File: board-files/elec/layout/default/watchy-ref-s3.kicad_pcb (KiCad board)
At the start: 4 copper layers, 33.8 x 46 mm, 70 parts, among them J1 FPC24(0.5MM), J2 Micro USB, J3 Battery, M1 Vibration_Motor, Q1 AO3400A, Q2 UMH3N, Q4 CJ2301, Q5 S8050, SW1 BTN, SW2 BTN, SW3 BTN, SW4 BTN, U1 ESP32-PICO-D4, U2 ME6211C33M5G-N, U3 CP2102, U4 BMA423, U5 TP4054, U6 PCF8563BS, Y1 32.768KHz

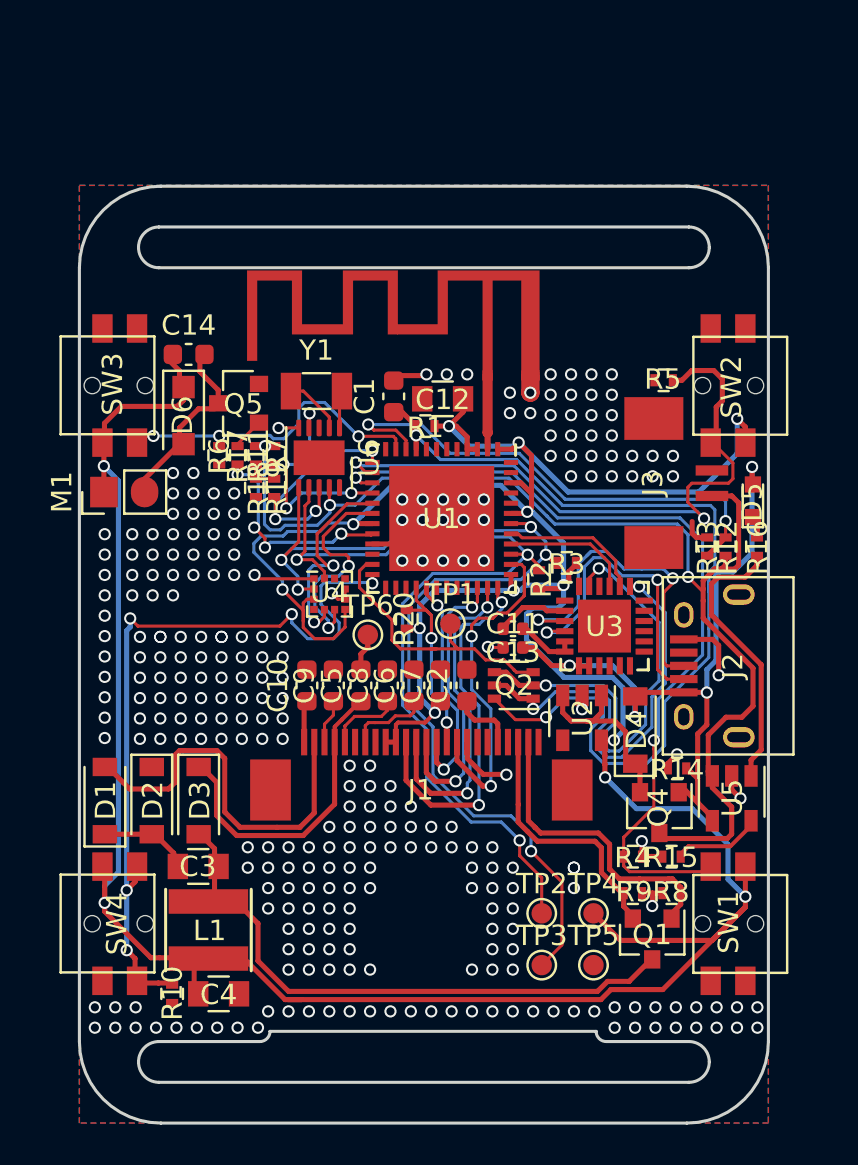
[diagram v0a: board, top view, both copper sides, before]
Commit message: board: apply the netlist to the PCB headlessly, and verify it
KiCad's netlist import is a GUI dialog and kicad-cli has no equivalent, so
scripts/apply_netlist.py does that job with pcbnew. The part that mattered
was preserving placement: V2's footprints carry KiCad 5 library names, so a
naive delete-and-re-add loses V2's coordinates for 39 parts over what is
mostly just a rename. It now records each pose and restores it.

It also adds and places the new parts, assigns all 249 pads across 73 nets,
lays the GND and +3V3 pour outlines, and nudges the small parts it placed
off their neighbours on a spiral search. The module goes 7.7mm below the top
edge so Espressif's antenna keepout -- which forbids pour on every layer --
hangs off the board.

scripts/check_board.py verifies the result independently and is wired into
checks/run.sh. Both it and the netlist assertions are mutation-tested.

Seven courtyard overlaps are left for a human and reported with their depth:
the 15.4x20.5mm module lands on C12, C1, R1, R7 and Q5 where V2 had a 7x7
QFN, and the USB-C lands on D4 and U2. Where those parts move is a design
decision, not arithmetic. Nothing is routed.
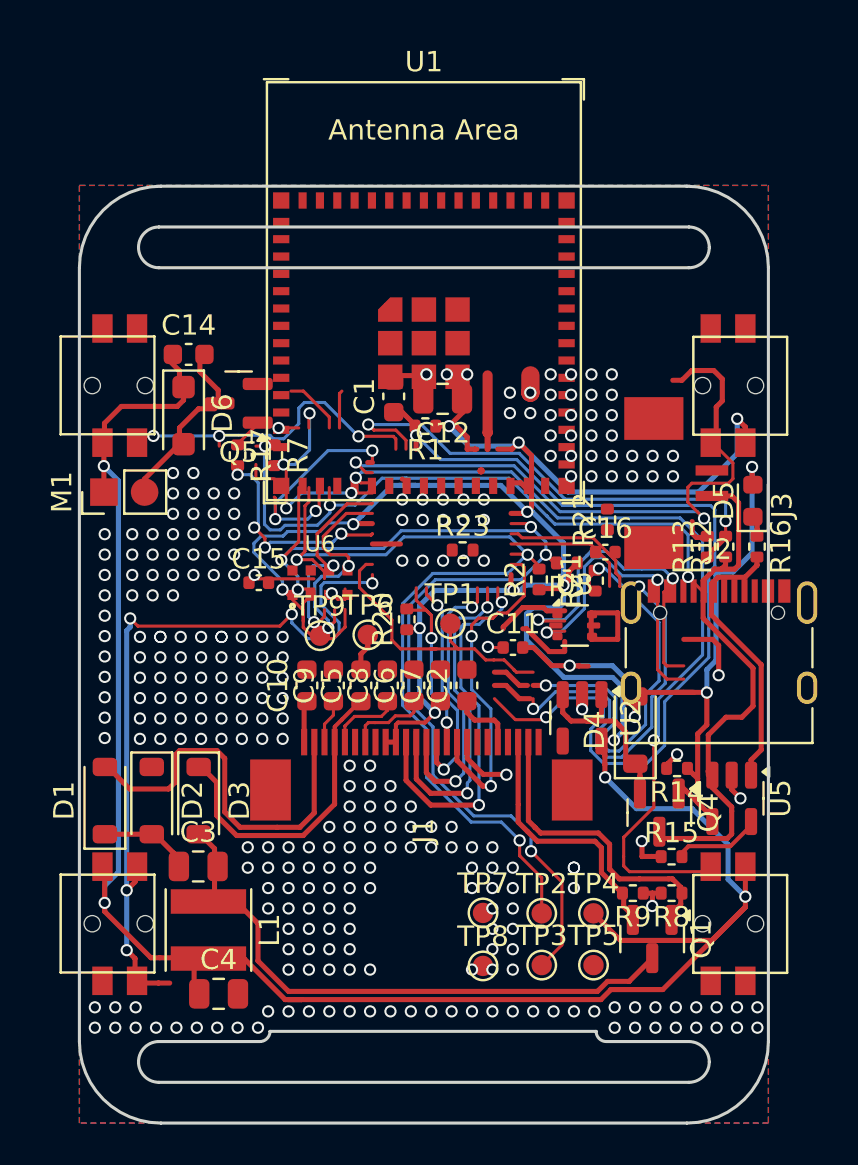
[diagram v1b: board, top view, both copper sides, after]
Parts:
- removed AE1: SWRA117D, Watchy:SWRA117D
- removed C13: 4.7uF, Capacitor_SMD:C_0402_1005Metric
- removed Q2: UMH3N, TO_SOT_Packages_SMD:SOT-363_SC-70-6
- removed R10, R4, R5, R6: 10K, Resistors_SMD:R_0402
- removed R11: 680K, Watchy:R_0402
- removed R18: 220K, Watchy:R_0402
- removed R19: 100K, Watchy:R_0402
- removed U4: BMA423, Housings_LGA:LGA-12_2x2mm_Pitch0.5mm
- removed Y1: 32.768KHz, Crystal:Crystal_SMD_3215-2Pin_3.2x1.5mm
- added C15: 100nF, C_0402_1005Metric, F.Cu at (77.5, 89.6)
- added C16: 100nF, C_0402_1005Metric, F.Cu at (94.5, 88.1)
- added R21: 5.1k, R_0402_1005Metric, F.Cu at (94.0, 89.5)
- added R22: 5.1k, R_0402_1005Metric, F.Cu at (94.6, 86.5)
- added R23: 10k, R_0402_1005Metric, F.Cu at (87.5, 88.0)
- added TP7: 1.0mm test pad, TestPoint_Pad_D1.0mm, F.Cu at (88.5, 105.8)
- added TP8: 1.0mm test pad, TestPoint_Pad_D1.0mm, F.Cu at (88.5, 108.4)
- added TP9: 1.0mm test pad, TestPoint_Pad_D1.0mm, F.Cu at (80.5, 92.2)
- C12, C3, C4: footprint Capacitors_SMD:C_0805 -> C_0805_2012Metric
- D1, D2, D3, D4: value MBR0530 -> MBR0530 Schottky; footprint Diodes_SMD:D_SOD-123 -> D_SOD-123
- D5: value LED -> LED (charge status); footprint LEDs:LED_0603 -> LED_0603_1608Metric
- D6: footprint Diodes_SMD:D_SOD-123F -> D_SOD-123F
- J1: value FPC24(0.5MM) -> FPC24 0.5mm ZIF; footprint Watchy:24_Pins_0.5mm_Pitch_ZIF_Connector_UP -> 24_Pins_0.5mm_Pitch_ZIF_Connector_UP
- J2: value Micro USB -> USB-C 2.0 receptacle, 16 pin; footprint Watchy:USB_Micro-B -> USB_C_Receptacle_XKB_U262-16XN-4BVC11
- J3: value Battery -> JST 1.25mm battery connector; footprint Watchy:1.25T-2PWT (Molex 532610271) -> 1.25T-2PWT (Molex 532610271)
- L1: footprint Inductors:Inductor_Taiyo-Yuden_NR-40xx -> L_Taiyo-Yuden_NR-40xx
- M1: value Vibration_Motor -> Vibration motor pads; footprint Watchy:Motor_Header -> Motor_Header
- Q1: value AO3400A -> AO3400A N-channel MOSFET; footprint TO_SOT_Packages_SMD:SOT-23 -> SOT-23
- Q4: value CJ2301 -> CJ2301 P-channel MOSFET; footprint TO_SOT_Packages_SMD:SOT-23 -> SOT-23
- Q5: value S8050 -> S8050 NPN; footprint TO_SOT_Packages_SMD:SOT-23 -> SOT-23
- R1, R14, R15, R7, R8: value 10K -> 10k; footprint Resistors_SMD:R_0402 -> R_0402_1005Metric
- R12, R13: value 100K -> 1M; footprint Resistors_SMD:R_0402 -> R_0402_1005Metric
- R16, R17: value 1K -> 1k; footprint Resistors_SMD:R_0402 -> R_0402_1005Metric
- R2, R3: value 4.7K -> 4.7k; footprint Resistors_SMD:R_0402 -> R_0402_1005Metric
- R20: value 100K -> 100k; footprint Watchy:R_0402 -> R_0402_1005Metric
- R9: value 3 -> 3R; footprint Resistors_SMD:R_0402 -> R_0402_1005Metric
- SW1, SW2, SW3, SW4: value BTN -> Side tactile switch; footprint Watchy:K2-1114SA-A4SW-06 -> K2-1114SA-A4SW-06
- U1: value ESP32-PICO-D4 -> ESP32-S3-MINI-1; footprint Housings_DFN_QFN:QFN-48-1EP_7x7mm_Pitch0.5mm -> ESP32-S3-MINI-1
- U2: value ME6211C33M5G-N -> ME6211C33M5G-N 3.3V LDO; footprint TO_SOT_Packages_SMD:SOT-23-5 -> SOT-23-5
- U3: value CP2102 -> USBLC6-2P6 USB ESD array; footprint Housings_DFN_QFN:QFN-24-1EP_4x4mm_Pitch0.5mm -> SOT-666
- U5: value TP4054 -> TP4054 Li-ion charger; footprint TO_SOT_Packages_SMD:SOT-23-5 -> SOT-23-5
- U6: value PCF8563BS -> RV-3028-C7 RTC; footprint Package_DFN_QFN:DFN-10-1EP_3x3mm_P0.5mm_EP1.7x2.5mm -> RV-3028-C7
- moved U1 8.65 mm to (85.6, 77.8), turned to 0 degrees
- moved U6 6.13 mm to (80.5, 89.6), turned to 0 degrees
- moved U3 1.46 mm to (93.0, 91.7)
- turned J2 to 0 degrees
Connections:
- net DC renamed EPD_DC
- net Net-(C10-Pad1) renamed EPD_C24
- net Net-(C14-Pad2) renamed MOTOR_DRV
- net Net-(C2-Pad1) renamed EPD_C5
- net Net-(C3-Pad1) renamed CP_NEG
- net Net-(C3-Pad2) renamed CP_POS
- net Net-(C6-Pad1) renamed EPD_C18
- net Net-(C8-Pad1) renamed EPD_C20
- net Net-(C9-Pad1) renamed EPD_C22
- net Net-(D4-Pad1) renamed VSYS
- net Net-(D5-Pad1) renamed LED_A
- net Net-(J1-Pad1) renamed net-1
- net Net-(J1-Pad19) renamed net-5
- net Net-(J1-Pad4) renamed net-2
- net Net-(J1-Pad6) renamed net-3
- net Net-(J1-Pad7) renamed net-4
- net Net-(Q5-Pad1) renamed VIB_BASE
- net Net-(R15-Pad2) renamed PROG
- net Net-(R16-Pad2) renamed CHRG
- net Net-(U1-Pad22) renamed io18
- net Net-(U1-Pad25) renamed io21
- net Net-(U1-Pad26) renamed io26
- net Net-(U1-Pad33) renamed io37
- net Net-(U1-Pad44) renamed io46
- net Net-(U1-Pad5) renamed io1
- net Net-(U1-Pad6) renamed io2
- net Net-(U1-Pad7) renamed io3
- net Net-(U2-Pad4) renamed net
- J1 pad 10: RES -> EPD_RST
- J1 pad 12: SS -> EPD_CS
- J1 pad 13: SCK -> EPD_SCK
- J1 pad 14: MOSI -> EPD_MOSI
- J1 pad 9: BUSY -> EPD_BUSY
- J1 pad M: (no net) -> net-6
- R12 pad 2: ADC -> BATT_ADC
- R13 pad 1: ADC -> BATT_ADC
- R20 pad 2: RES -> EPD_RST
- R7 pad 1: +BATT -> +3V3
- SW1 pad 1: +3V3 -> GND
- SW1 pad 2: BTN_1 -> BTN_MENU
- SW2 pad 1: +3V3 -> GND
- SW2 pad 2: BTN_2 -> BTN_BACK
- SW3 pad 1: +3V3 -> GND
- SW3 pad 2: BTN_3 -> BTN_UP
- SW4 pad 1: +3V3 -> GND
- SW4 pad 2: BTN_4 -> BTN_DOWN
- TP1 pad 1: GPIO0 -> TP_BOOT
- U1 pad 1: +3V3 -> GND
- U1 pad 10: ADC -> BTN_UP
- U1 pad 11: BTN_3 -> BTN_DOWN
- U1 pad 12: Net-(U1-Pad12) -> RTC_INT
- U1 pad 13: 32KHZ -> BATT_ADC
- U1 pad 14: BTN_2 -> io10
- U1 pad 15: BTN_1 -> SCL
- U1 pad 16: RTC_INT -> SDA
- U1 pad 17: ACC_INT_1 -> io13
- U1 pad 18: ACC_INT_2 -> io14
- U1 pad 19: +3V3 -> io15
- U1 pad 2: Net-(AE1-Pad1) -> GND
- U1 pad 20: VIB_PWM -> io16
- U1 pad 21: GND -> VIB_PWM
- U1 pad 23: GPIO0 -> USB_DM
- U1 pad 24: BTN_4 -> USB_DP
- U1 pad 27: Net-(U1-Pad27) -> EPD_SCK
- U1 pad 28: RES -> EPD_CS
- U1 pad 30: Net-(U1-Pad30) -> EPD_MOSI
- U1 pad 31: Net-(U1-Pad31) -> EPD_RST
- U1 pad 32: Net-(U1-Pad32) -> EPD_BUSY
- U1 pad 34: SS -> io38
- U1 pad 35: SCK -> io39
- U1 pad 36: MOSI -> io40
- U1 pad 37: +3V3 -> io41
- U1 pad 38: BUSY -> io42
- U1 pad 39: SCL -> TP_TX
- U1 pad 4: +3V3 -> TP_BOOT
- U1 pad 40: RX -> TP_RX
- U1 pad 41: TX -> io45
- U1 pad 42: SDA -> GND
- U1 pad 43: +3V3 -> GND
- U1 pad 45: Net-(U1-Pad45) -> EN
- U1 pad 46: +3V3 -> GND
- U1 pad 47: Net-(U1-Pad47) -> GND
- U1 pad 48: Net-(U1-Pad48) -> GND
- U1 pad 8: Net-(U1-Pad8) -> BTN_MENU
- U1 pad 9: EN -> BTN_BACK
- U3 pad 1: Net-(U3-Pad1) -> USB_DP
- U3 pad 3: Net-(J2-Pad3) -> USB_DM
- U3 pad 4: Net-(J2-Pad2) -> USB_DM
- U3 pad 5: Net-(C13-Pad1) -> VBUS
- U3 pad 6: Net-(C13-Pad1) -> USB_DP
- U6 pad 1: Net-(U6-Pad1) -> RTC_CLKOUT
- U6 pad 2: Net-(U6-Pad2) -> RTC_INT
- U6 pad 3: Net-(U6-Pad3) -> SCL
- U6 pad 4: RTC_INT -> SDA
- U6 pad 6: SDA -> GND
- U6 pad 7: SCL -> +BATT
- U6 pad 8: 32KHZ -> GND
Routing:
- net BTN_DOWN: track 0.00 -> 38.1 mm, vias 0 -> 5
- net BTN_4: track 38.1 -> 0.00 mm, vias 5 -> 0
- net BTN_BACK: track 0.00 -> 31.2 mm, vias 0 -> 2
- net BTN_2: track 31.2 -> 0.00 mm, vias 2 -> 0
- net BATT_ADC: track 0.00 -> 24.6 mm, vias 0 -> 2
- net ADC: track 24.6 -> 0.00 mm, vias 2 -> 0
- net MOSI: track 19.0 -> 0.00 mm, vias 2 -> 0
- net EPD_MOSI: track 0.00 -> 19.0 mm, vias 0 -> 2
- net EPD_BUSY: track 0.00 -> 18.8 mm, vias 0 -> 2
- net BUSY: track 18.8 -> 0.00 mm, vias 2 -> 0
- net SCK: track 16.5 -> 0.00 mm, vias 2 -> 0
- net EPD_SCK: track 0.00 -> 16.5 mm, vias 0 -> 2
- net SS: track 14.5 -> 0.00 mm, vias 2 -> 0
- net EPD_CS: track 0.00 -> 14.5 mm, vias 0 -> 2
- net TP_BOOT: track 0.00 -> 14.1 mm
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- added copper zone on In2.Cu, net +3V3
- added copper zone on In1.Cu, net GND

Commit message: board: place the displaced parts by anchoring them to the pad they serve
The module and the USB-C displaced seven of V2's parts. Rather than reporting
them and stopping, apply_netlist.py now anchors each to the pad it actually
serves -- C12 to the module's 3V3 pad, C1 and R1 to EN, R7 to the RTC's INT
pin, Q5 to the motor pads, U2 and D4 to Q4 -- and takes the nearest clear
spot to it. Five land within 3.5mm. U2 and D4 land 11mm and 12.8mm out
because the area around the charger is dense; both carry DC rather than a
switching node, and the report flags anything past 5mm rather than hiding it
in a number.

Relocation only fires for a part that is actually overlapping something, so
re-running over a board someone has been editing does not undo their
placement.

Two bugs found while doing this. The overlap report diffed against the board
file the script itself had written, so after one run it excused its own
overlaps as "V2 already had this"; it now diffs against a committed,
untouched copy of V2's converted layout. And overlaps involving a part this
run replaced or moved were being waved through under V2's name; they are now
listed separately for review.

What remains is nine overlaps of 0.10-0.23mm between untouched V2 parts,
caused by KiCad 7 footprints being fractionally larger than KiCad 5's.
Still nothing routed.
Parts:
- moved D4 14.8 mm to (86.2, 107.9)
- moved C1 13.5 mm to (94.6, 71.9)
- moved C12 13.0 mm to (75.6, 73.6)
- moved R1 12.0 mm to (94.6, 73.9)
- moved U2 10.5 mm to (85.7, 103.4)
- moved Q5 9.11 mm to (71.9, 88.7)
- moved R7 8.39 mm to (79.0, 91.7)
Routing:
- net BTN_DOWN: track 38.1 -> 0.00 mm, vias 5 -> 0
- net BTN_4: track 0.00 -> 38.1 mm, vias 0 -> 5
- net Net-(C3-Pad2): track 0.00 -> 30.2 mm
- net CP_POS: track 30.2 -> 0.00 mm
- net Net-(D4-Pad1): track 0.00 -> 7.16 mm
- net VSYS: track 8.26 -> 1.10 mm
- net VIB_BASE: track 0.00 -> 1.58 mm
- net Net-(Q5-Pad1): track 1.58 -> 0.00 mm
